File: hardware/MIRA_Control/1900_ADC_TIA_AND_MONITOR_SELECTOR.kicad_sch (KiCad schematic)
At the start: 32 parts, among them U1900 OPA551, U1901 ADG5408, U1902 ADG1208, U1903 OPA2197

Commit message: Add high-load schematic candidate with CORE sense and revised N15 supply
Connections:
- net MAT_CC_SENSE_BUF: now also U1903.2 (IN-)
- net MAT_ILIM_SENSE_BUF: now also U1903.6 (IN-)
- net V- renamed N15
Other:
- moved on the sheet: U1902
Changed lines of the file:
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@@
 	(wire
 		(pts
-			(xy 266.065 70.485) (xy 260.985 70.485)
+			(xy 266.7 71.12) (xy 261.62 71.12)
 		)
 		(stroke
@@
 	(wire
 		(pts
-			(xy 266.065 80.645) (xy 260.985 80.645)
+			(xy 266.7 81.28) (xy 261.62 81.28)
 		)
 		(stroke
@@
 	(wire
 		(pts
-			(xy 294.005 67.945) (xy 299.085 67.945)
+			(xy 294.64 68.58) (xy 299.72 68.58)
 		)
 		(stroke
@@
 	(wire
 		(pts
-			(xy 294.005 83.185) (xy 299.085 83.185)
+			(xy 294.64 83.82) (xy 299.72 83.82)
 		)
 		(stroke
@@
 	(wire
 		(pts
-			(xy 180.34 123.19) (xy 185.42 123.19)
+			(xy 180.34 123.19) (xy 182.88 123.19)
 		)
 		(stroke
@@
 	(wire
 		(pts
-			(xy 248.92 123.19) (xy 254 123.19)
+			(xy 248.92 123.19) (xy 251.46 123.19)
 		)
 		(stroke
@@
 	(wire
 		(pts
-			(xy 294.005 80.645) (xy 299.085 80.645)
+			(xy 294.64 81.28) (xy 299.72 81.28)
 		)
 		(stroke
@@
 	(wire
 		(pts
-			(xy 266.065 67.945) (xy 260.985 67.945)
+			(xy 266.7 68.58) (xy 261.62 68.58)
 		)
 		(stroke
@@
 	(wire
 		(pts
-			(xy 294.005 75.565) (xy 299.085 75.565)
+			(xy 294.64 76.2) (xy 299.72 76.2)
 		)
 		(stroke
@@
 	(wire
 		(pts
-			(xy 266.065 65.405) (xy 260.985 65.405)
+			(xy 266.7 66.04) (xy 261.62 66.04)
 		)
 		(stroke
@@
 	(wire
 		(pts
-			(xy 294.005 78.105) (xy 299.085 78.105)
+			(xy 294.64 78.74) (xy 299.72 78.74)
 		)
 		(stroke
@@
 	(wire
 		(pts
-			(xy 266.065 78.105) (xy 260.985 78.105)
+			(xy 266.7 78.74) (xy 261.62 78.74)
 		)
 		(stroke
@@
 	(wire
 		(pts
-			(xy 266.065 83.185) (xy 260.985 83.185)
+			(xy 266.7 83.82) (xy 261.62 83.82)
 		)
 		(stroke
@@
 	(wire
 		(pts
-			(xy 266.065 73.025) (xy 260.985 73.025)
+			(xy 266.7 73.66) (xy 261.62 73.66)
 		)
 		(stroke
@@
 	(wire
 		(pts
-			(xy 294.005 70.485) (xy 299.085 70.485)
+			(xy 294.64 71.12) (xy 299.72 71.12)
 		)
 		(stroke
@@
 	(wire
 		(pts
-			(xy 266.065 75.565) (xy 260.985 75.565)
+			(xy 266.7 76.2) (xy 261.62 76.2)
 		)
 		(stroke
@@
 	(wire
 		(pts
-			(xy 294.005 73.025) (xy 299.085 73.025)
+			(xy 294.64 73.66) (xy 299.72 73.66)
 		)
 		(stroke
@@
 	(wire
 		(pts
-			(xy 294.005 65.405) (xy 299.085 65.405)
+			(xy 294.64 66.04) (xy 299.72 66.04)
 		)
 		(stroke
@@
 	(global_label "MAT_TIA_OUT"
 		(shape bidirectional)
-		(at 260.985 65.405 180)
+		(at 261.62 66.04 180)
 		(effects
 			(font
@@
 		)
 		(property "Intersheetrefs" "${INTERSHEET_REFS}"
-			(at 260.985 65.405 0)
+			(at 261.62 66.04 0)
 			(hide yes)
 			(show_name no)
@@
 	(global_label "MAT_SENSE_A1"
 		(shape bidirectional)
-		(at 299.085 70.485 0)
+		(at 299.72 71.12 0)
 		(effects
 			(font
@@
 		)
 		(property "Intersheetrefs" "${INTERSHEET_REFS}"
-			(at 299.085 70.485 0)
+			(at 299.72 71.12 0)
 			(hide yes)
 			(show_name no)
@@
 	(global_label "IO3V3"
 		(shape bidirectional)
-		(at 299.085 75.565 0)
+		(at 299.72 76.2 0)
 		(effects
 			(font
@@
 		)
 		(property "Intersheetrefs" "${INTERSHEET_REFS}"
-			(at 299.085 75.565 0)
+			(at 299.72 76.2 0)
 			(hide yes)
 			(show_name no)
@@
 	(global_label "N15"
 		(shape bidirectional)
-		(at 299.085 80.645 0)
+		(at 299.72 81.28 0)
 		(effects
 			(font
@@
 		)
 		(property "Intersheetrefs" "${INTERSHEET_REFS}"
-			(at 299.085 80.645 0)
+			(at 299.72 81.28 0)
 			(hide yes)
 			(show_name no)
@@
 	(global_label "MAT_SENSE_A0"
 		(shape bidirectional)
-		(at 299.085 67.945 0)
+		(at 299.72 68.58 0)
 		(effects
 			(font
@@
 		)
 		(property "Intersheetrefs" "${INTERSHEET_REFS}"
-			(at 299.085 67.945 0)
+			(at 299.72 68.58 0)
 			(hide yes)
 			(show_name no)
@@
 	(global_label "MAT_ILIM_SENSE_BUF"
 		(shape bidirectional)
-		(at 260.985 75.565 180)
+		(at 261.62 76.2 180)
 		(effects
 			(font
@@
 		)
 		(property "Intersheetrefs" "${INTERSHEET_REFS}"
-			(at 260.985 75.565 0)
+			(at 261.62 76.2 0)
 			(hide yes)
 			(show_name no)
@@
 	(global_label "GND"
 		(shape bidirectional)
-		(at 260.985 83.185 180)
+		(at 261.62 83.82 180)
 		(effects
 			(font
@@
 		)
 		(property "Intersheetrefs" "${INTERSHEET_REFS}"
-			(at 260.985 83.185 0)
+			(at 261.62 83.82 0)
 			(hide yes)
 			(show_name no)
@@
 	(global_label "P15"
 		(shape bidirectional)
-		(at 299.085 78.105 0)
+		(at 299.72 78.74 0)
 		(effects
 			(font
@@
 		)
 		(property "Intersheetrefs" "${INTERSHEET_REFS}"
-			(at 299.085 78.105 0)
+			(at 299.72 78.74 0)
 			(hide yes)
 			(show_name no)
@@
 	(global_label "MAT_MONITOR_RAW"
 		(shape bidirectional)
-		(at 299.085 65.405 0)
+		(at 299.72 66.04 0)
 		(effects
 			(font
@@
 		)
 		(property "Intersheetrefs" "${INTERSHEET_REFS}"
-			(at 299.085 65.405 0)
+			(at 299.72 66.04 0)
 			(hide yes)
 			(show_name no)
@@
 	(global_label "MAT_CC_SENSE_BUF"
 		(shape bidirectional)
-		(at 260.985 73.025 180)
+		(at 261.62 73.66 180)
 		(effects
 			(font
@@
 		)
 		(property "Intersheetrefs" "${INTERSHEET_REFS}"
-			(at 260.985 73.025 0)
+			(at 261.62 73.66 0)
 			(hide yes)
 			(show_name no)
@@
 	(global_label "GND"
 		(shape bidirectional)
-		(at 299.085 83.185 0)
+		(at 299.72 83.82 0)
 		(effects
 			(font
@@
 		)
 		(property "Intersheetrefs" "${INTERSHEET_REFS}"
-			(at 299.085 83.185 0)
+			(at 299.72 83.82 0)
 			(hide yes)
 			(show_name no)
@@
 	(global_label "MAT_SENSE_A2"
 		(shape bidirectional)
-		(at 299.085 73.025 0)
+		(at 299.72 73.66 0)
 		(effects
 			(font
@@
 		)
 		(property "Intersheetrefs" "${INTERSHEET_REFS}"
-			(at 299.085 73.025 0)
+			(at 299.72 73.66 0)
 			(hide yes)
 			(show_name no)
@@
 	(global_label "GND"
 		(shape bidirectional)
-		(at 260.985 80.645 180)
+		(at 261.62 81.28 180)
 		(effects
 			(font
@@
 		)
 		(property "Intersheetrefs" "${INTERSHEET_REFS}"
-			(at 260.985 80.645 0)
+			(at 261.62 81.28 0)
 			(hide yes)
 			(show_name no)
@@
 	(global_label "GND"
 		(shape bidirectional)
-		(at 260.985 78.105 180)
+		(at 261.62 78.74 180)
 		(effects
 			(font
@@
 		)
 		(property "Intersheetrefs" "${INTERSHEET_REFS}"
-			(at 260.985 78.105 0)
+			(at 261.62 78.74 0)
 			(hide yes)
 			(show_name no)
@@
 	(global_label "MAT_BL_SERVICE"
 		(shape bidirectional)
-		(at 260.985 67.945 180)
+		(at 261.62 68.58 180)
 		(effects
 			(font
@@
 		)
 		(property "Intersheetrefs" "${INTERSHEET_REFS}"
-			(at 260.985 67.945 0)
+			(at 261.62 68.58 0)
 			(hide yes)
 			(show_name no)
@@
 	(global_label "MAT_NL_SERVICE"
 		(shape bidirectional)
-		(at 260.985 70.485 180)
+		(at 261.62 71.12 180)
 		(effects
 			(font
@@
 		)
 		(property "Intersheetrefs" "${INTERSHEET_REFS}"
-			(at 260.985 70.485 0)
+			(at 261.62 71.12 0)
 			(hide yes)
 			(show_name no)
@@
 	(symbol
 		(lib_id "MIRA_RevA:ADG1208_MIRA_MAT")
-		(at 280.035 74.295 0)
+		(at 280.67 74.93 0)
 		(unit 1)
 		(body_style 1)
@@
 		(dnp no)
 		(property "Reference" "U1902"
-			(at 280.035 89.995 0)
+			(at 280.67 90.63 0)
 			(show_name no)
 			(do_not_autoplace no)
@@
 		)
 		(property "Value" "ADG1208"
-			(at 280.035 92.495 0)
+			(at 280.67 93.13 0)
 			(show_name no)
 			(do_not_autoplace no)
@@
 		)
 		(property "Footprint" "MIRA_RevA:TSSOP-16_4.4x5mm_P0.65mm"
-			(at 280.035 74.295 0)
+			(at 280.67 74.93 0)
 			(hide yes)
 			(show_name no)
@@
 		)
 		(property "Datasheet" "https://www.analog.com/media/en/technical-documentation/data-sheets/adg1208_1209.pdf"
-			(at 280.035 74.295 0)
+			(at 280.67 74.93 0)
 			(hide yes)
 			(show_name no)
@@
 		)
 		(property "Description" "ADG1208"
-			(at 280.035 74.295 0)
+			(at 280.67 74.93 0)
 			(hide yes)
 			(show_name no)
@@
 		)
 		(property "MPN" "ADG1208YRUZ"
-			(at 280.035 74.295 0)
+			(at 280.67 74.93 0)
 			(hide yes)
 			(show_name no)
@@
 		)
 		(property "Manufacturer" "Analog Devices"
-			(at 280.035 74.295 0)
+			(at 280.67 74.93 0)
 			(hide yes)
 			(show_name no)
@@
 		)
 	)
+(wire (pts (xy 182.88 123.19) (xy 185.42 123.19)) (stroke (width 0) (type default)))
+(junction (at 182.88 123.19) (diameter 0) (color 0 0 0 0))
+(wire (pts (xy 251.46 123.19) (xy 254 123.19)) (stroke (width 0) (type default)))
+(junction (at 251.46 123.19) (diameter 0) (color 0 0 0 0))
 )

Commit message: Protect unpowered signal domains and qualify local supplies; retain startup and fault interlocks
MIRA-Startup-Patch: 7ffae17756ebcf923eff1212bb1aade8fbdfae03a9ca8ecebc69d3da3d3b4ba2
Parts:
- U1901: value ADG5408 -> TMUX7208PWR; symbol MIRA_RevA:ADG5408_MIRA_MAT -> MIRA_RevA:TMUX7208PWR_SIGNAL_MIRA; MPN ADG5408BRUZ -> TMUX7208PWR; Manufacturer Analog Devices -> Texas Instruments
- U1902: value ADG1208 -> TMUX7208PWR; symbol MIRA_RevA:ADG1208_MIRA_MAT -> MIRA_RevA:TMUX7208PWR_SIGNAL_MIRA; MPN ADG1208YRUZ -> TMUX7208PWR; Manufacturer Analog Devices -> Texas Instruments

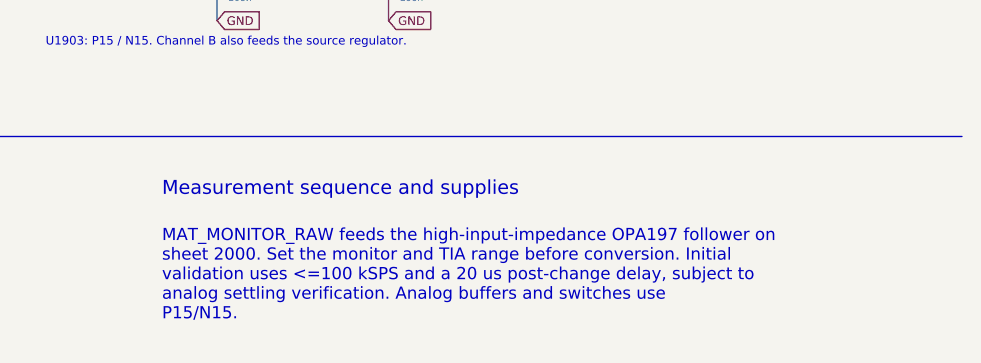
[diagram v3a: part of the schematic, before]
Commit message: MIRA.05: analog requirements and schematic fixes
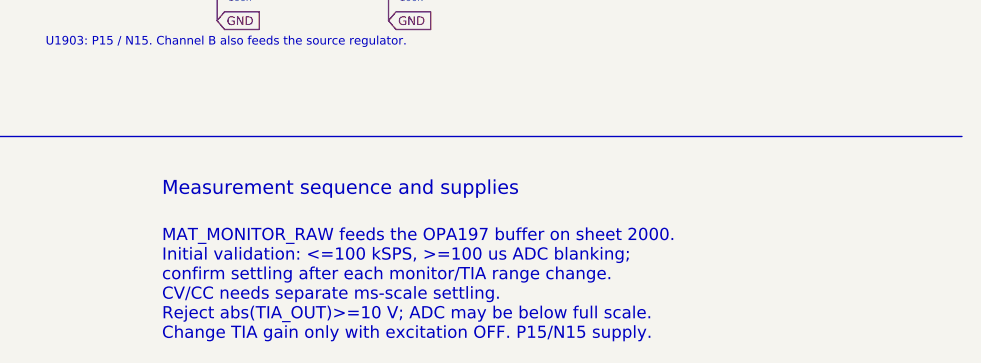
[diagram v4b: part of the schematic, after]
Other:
- note added: "MAT_MONITOR_RAW feeds the OPA197 buffer on sheet 2000. Initial validation: <=100 kSPS, >=100 us ADC blanking; confirm settling after each monitor/TIA range change. CV/CC needs separate ms-scale settling. Reject abs(TIA_OUT)>=10 V; ADC may be below full scale. Change TIA gain only with excitation OFF. P15/N15 supply."
- note removed: "MAT_MONITOR_RAW feeds the high-input-impedance OPA197 follower on sheet 2000. Set the monitor and TIA range before conversion. Initial validation uses <=100 kSPS and a 20 us post-change delay, subject to analog settling verification. Analog buffers and switches use P15/N15."
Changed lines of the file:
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@@
 		)
 	)
-	(text "MAT_MONITOR_RAW feeds the high-input-impedance OPA197 follower on\nsheet 2000. Set the monitor and TIA range before conversion. Initial\nvalidation uses <=100 kSPS and a 20 us post-change delay, subject to\nanalog settling verification. Analog buffers and switches use\nP15/N15."
-		(exclude_from_sim no)
-		(at 310.11 174.34 0)
-		(effects
-			(font
-				(size 1.35 1.35)
-				(color 0 70 160 1)
-			)
-			(justify left top)
-		)
-	)
+	(text "MAT_MONITOR_RAW feeds the OPA197 buffer on sheet 2000.\nInitial validation: <=100 kSPS, >=100 us ADC blanking;\nconfirm settling after each monitor/TIA range change.\nCV/CC needs separate ms-scale settling.\nReject abs(TIA_OUT)>=10 V; ADC may be below full scale.\nChange TIA gain only with excitation OFF. P15/N15 supply." (exclude_from_sim no) (at 310.11 174.34 0) (effects (font (size 1.35 1.35) (color 0 70 160 1)) (justify left top)))
 	(text "7"
 		(exclude_from_sim no)

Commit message: Review MIRA.06 components, connectors and assembly
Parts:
- C1900, C1902, C1905, C1906, C1915, C1916: MPN (none) -> CC0603KRX7R9BB104; Manufacturer Murata -> YAGEO
- C1901, C1904: MPN (none) -> CC1206KKX7R9BB475; Manufacturer Murata -> YAGEO
- C1903: MPN (none) -> CC0603CRNPO9BN2R2; Manufacturer Murata -> YAGEO
- C1907, C1912, C1913, C1914: MPN (none) -> CC0603JRNPO9BN331; Manufacturer Murata -> YAGEO
- C1908: MPN (none) -> CC0603JRNPO9BN101; Manufacturer Murata -> YAGEO
- C1909: MPN (none) -> CC0603JRNPO9BN330; Manufacturer Murata -> YAGEO
- C1910: MPN (none) -> CC0603JRNPO9BN100; Manufacturer Murata -> YAGEO
- C1911: MPN (none) -> CC0603CRNPO9BN3R3; Manufacturer Murata -> YAGEO
- C1917, C1918: MPN (none) -> CC0402KRX7R9BB104; Manufacturer TDK -> YAGEO
- R1900: MPN (none) -> RC0402FR-0710ML; Manufacturer Yageo -> YAGEO
- R1902: MPN (none) -> RT0603BRD071KL; Manufacturer Yageo -> YAGEO
- R1903: MPN (none) -> RT0603BRD0710KL; Manufacturer Yageo -> YAGEO
- R1904: MPN (none) -> RT0603BRD07100KL; Manufacturer Yageo -> YAGEO
- R1905: MPN (none) -> RT0603BRD071ML; Manufacturer Yageo -> YAGEO
